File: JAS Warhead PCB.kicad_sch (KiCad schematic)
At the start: 7 parts, among them J1 Conn_01x15_Socket, J2 Conn_01x15_Socket, J3 Conn_01x02_Socket, J4 Conn_01x02_Socket, J5 Conn_01x02_Socket, J6 Conn_01x02_Socket, J7 Conn_01x02_Socket

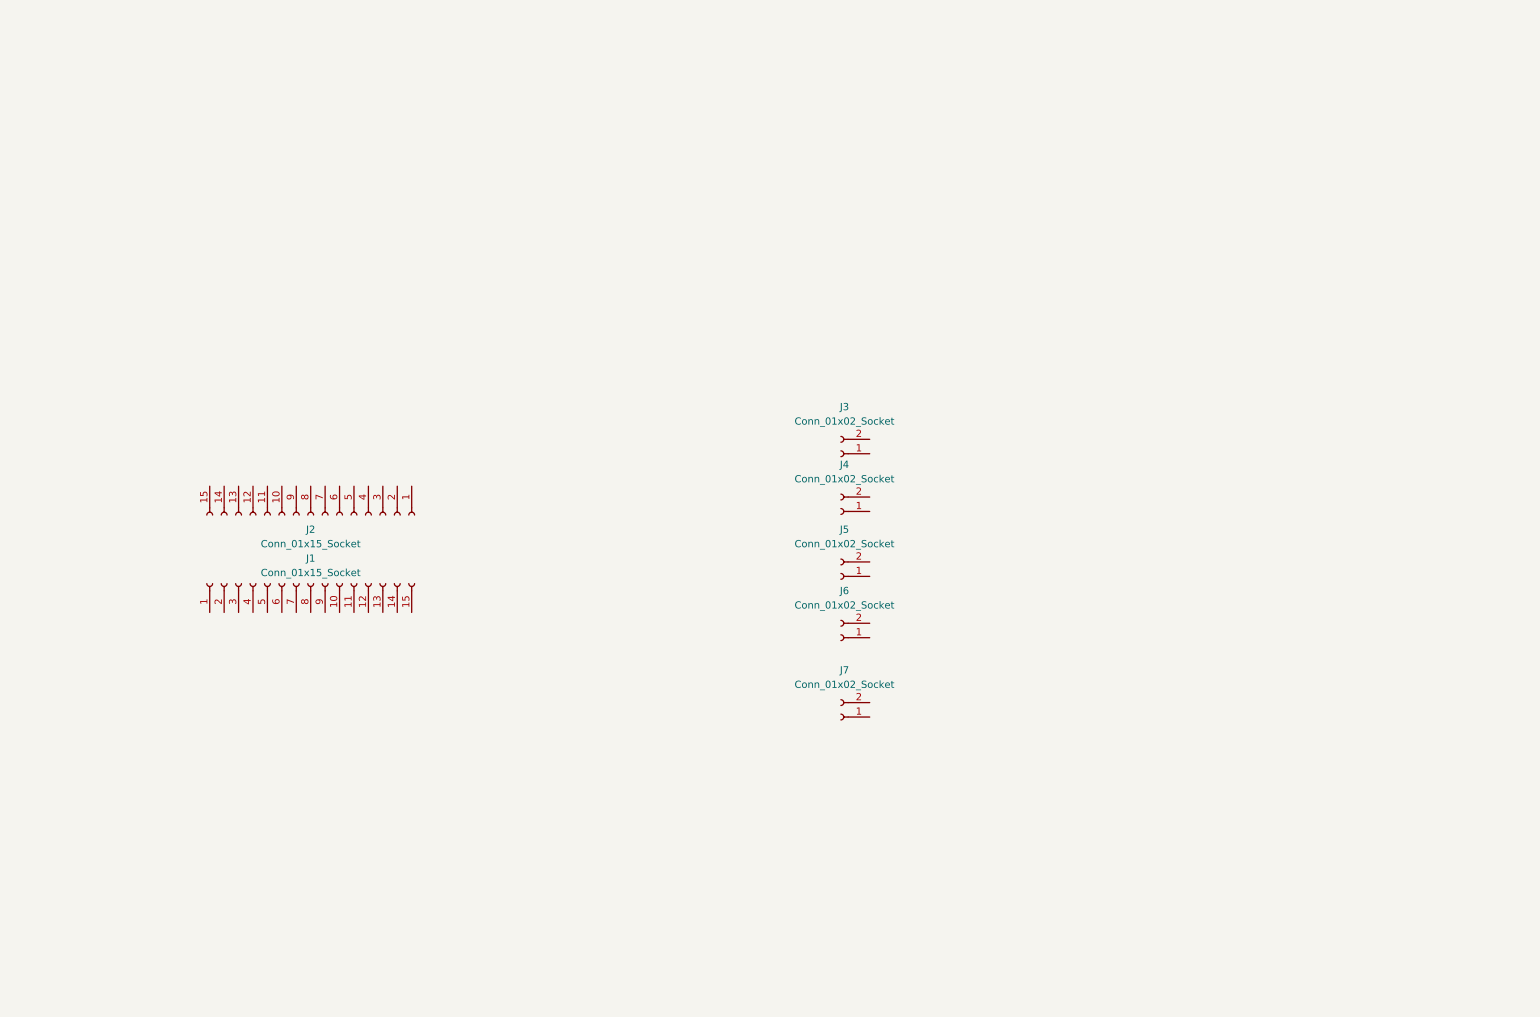
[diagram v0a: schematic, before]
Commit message: adds MAX31855 SPI K-Type Thermocouple Amps
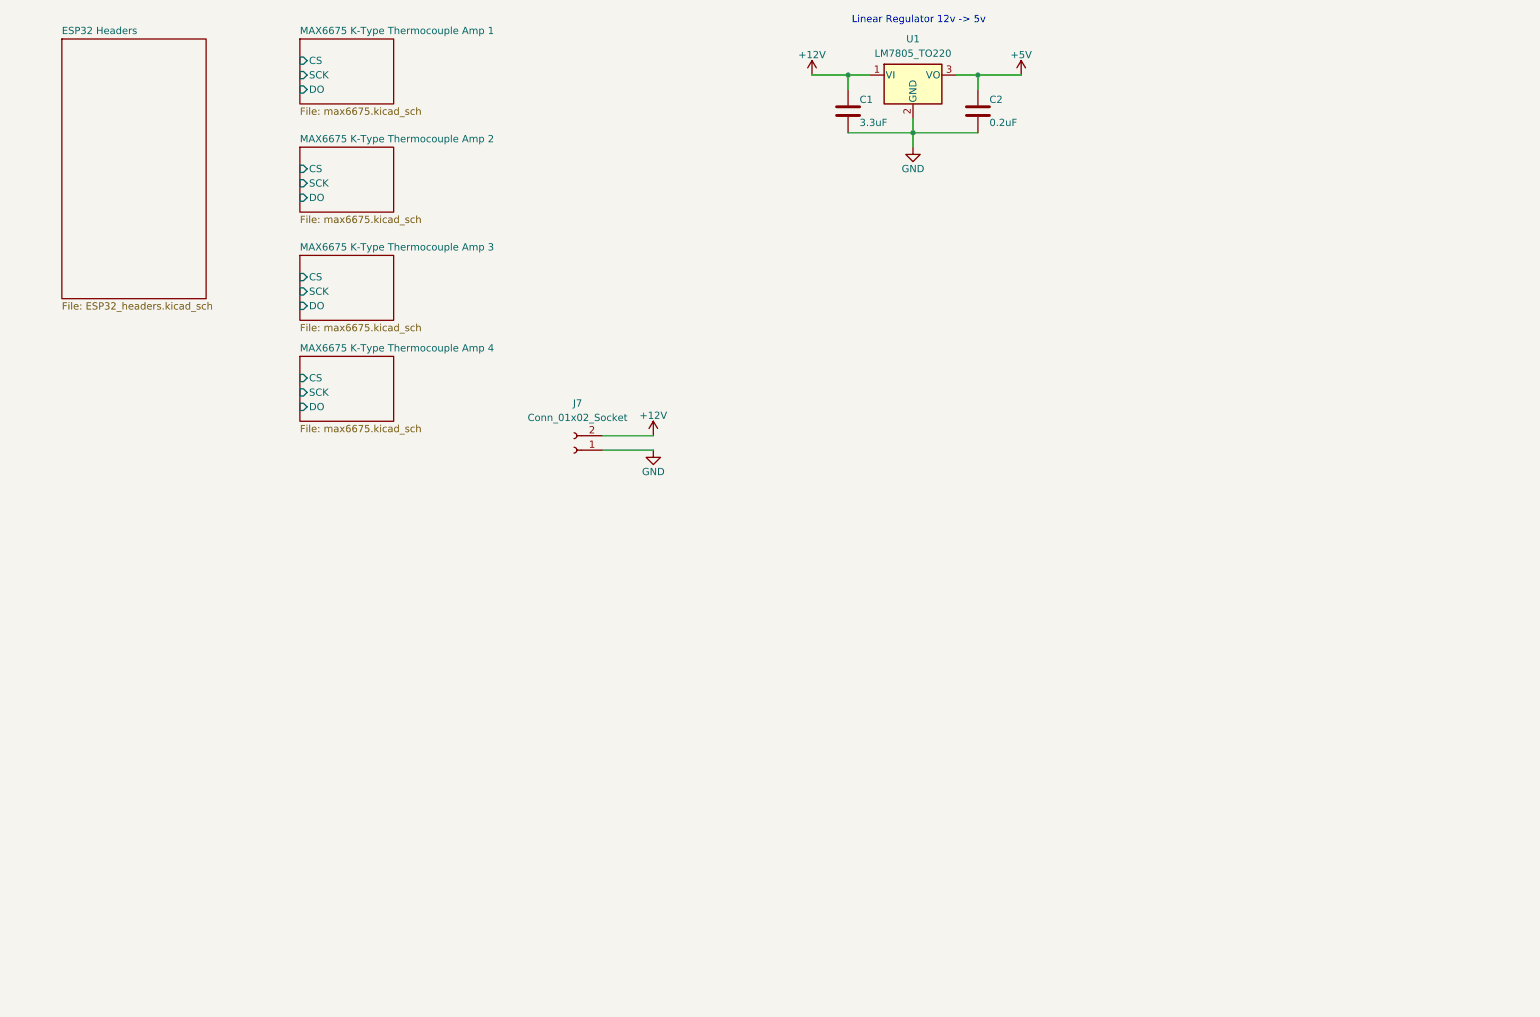
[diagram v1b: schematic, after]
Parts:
- removed J1, J2: Conn_01x15_Socket, Connector_PinSocket_2.54mm:PinSocket_1x15_P2.54mm_Vertical, symbol Connector:Conn_01x15_Socket
- removed J3, J4, J5, J6: Conn_01x02_Socket, TerminalBlock_4Ucon:TerminalBlock_4Ucon_1x02_P3.50mm_Horizontal, symbol Connector:Conn_01x02_Socket
- added C1: 3.3uF, Capacitor_SMD:C_0504_1310Metric, symbol Device:C
- added C2: 0.2uF, Capacitor_SMD:C_0402_1005Metric, symbol Device:C
- added U1: LM7805_TO220, Package_TO_SOT_THT:TO-220-3_Vertical, symbol Regulator_Linear:LM7805_TO220
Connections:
- net GND: now reaches J7.1 (Pin_1)
- net GND: now also C1.2, C2.2, U1.2 (GND)
- net +12V: now reaches J7.2 (Pin_2)
- net +12V: now also C1.1, U1.1 (VI)
- new net +5V: C2.1, U1.3 (VO)
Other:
- added sheet ESP32 Headers (ESP32_headers.kicad_sch)
- added sheet MAX6675 K-Type Thermocouple Amp 1 (max6675.kicad_sch)
- added sheet MAX6675 K-Type Thermocouple Amp 2 (max6675.kicad_sch)
- added sheet MAX6675 K-Type Thermocouple Amp 3 (max6675.kicad_sch)
- added sheet MAX6675 K-Type Thermocouple Amp 4 (max6675.kicad_sch)
- note added: "Linear Regulator 12v -> 5v"
- moved on the sheet: J7

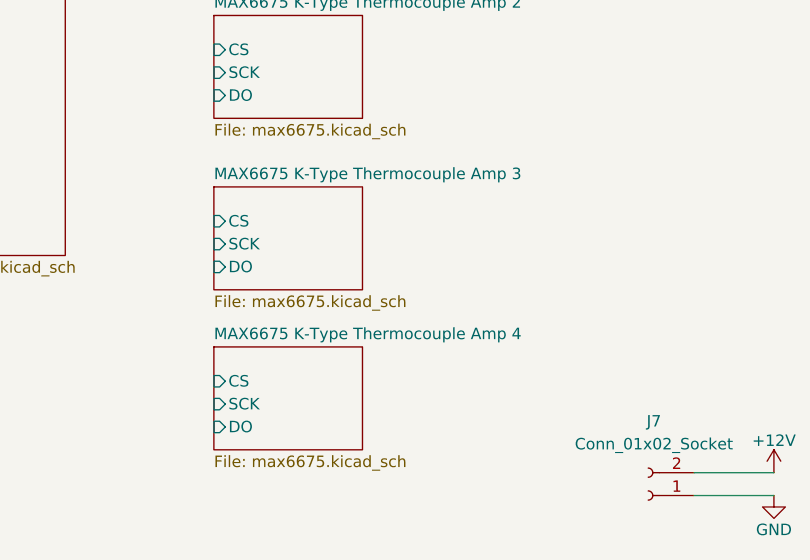
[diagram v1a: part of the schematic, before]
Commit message: finalizes MAX boards & Begins PCB Design
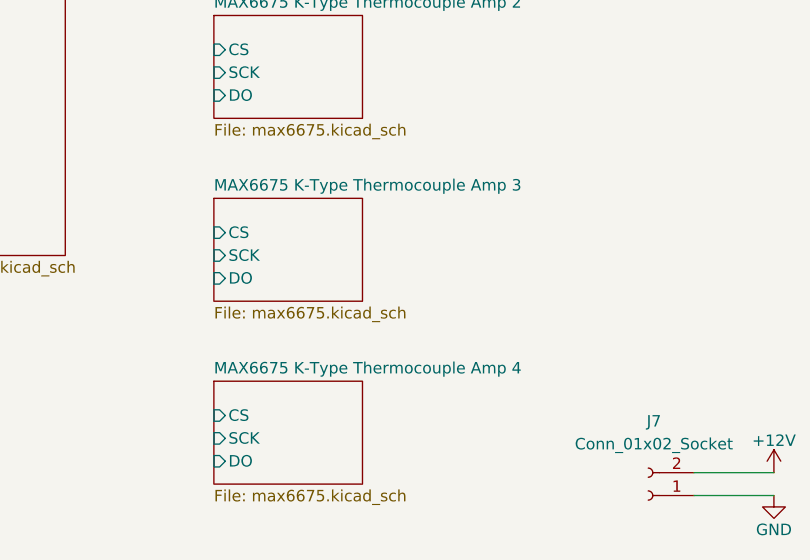
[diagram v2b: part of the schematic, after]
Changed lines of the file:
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@@
 	)
 	(sheet
-		(at 69.85 76.2)
+		(at 69.85 39.37)
+		(size 16.51 11.43)
+		(fields_autoplaced yes)
+		(stroke
+			(width 0.1524)
+			(type solid)
+		)
+		(fill
+			(color 0 0 0 0.0000)
+		)
+		(property "Sheetname" "MAX6675 K-Type Thermocouple Amp 2"
+			(at 69.85 38.6584 0)
+			(effects
+				(font
+					(size 1.27 1.27)
+				)
+				(justify left bottom)
+			)
+		)
+		(property "Sheetfile" "max6675.kicad_sch"
+			(at 69.85 51.3846 0)
+			(effects
+				(font
+					(size 1.27 1.27)
+				)
+				(justify left top)
+			)
+		)
+		(pin "CS" input
+			(at 69.85 43.18 180)
+			(effects
+				(font
+					(size 1.27 1.27)
+				)
+				(justify left)
+			)
+		)
+		(pin "SCK" input
+			(at 69.85 45.72 180)
+			(effects
+				(font
+					(size 1.27 1.27)
+				)
+				(justify left)
+			)
+		)
+		(pin "DO" input
+			(at 69.85 48.26 180)
+			(effects
+				(font
+					(size 1.27 1.27)
+				)
+				(justify left)
+			)
+		)
+		(instances
+			(project "JAS Warhead PCB"
+				(path "/a037544f-9a20-478c-bac0-d162f9edf245"
+					(page "4")
+				)
+			)
+		)
+	)
+	(sheet
+		(at 69.85 59.69)
+		(size 16.51 11.43)
+		(fields_autoplaced yes)
+		(stroke
+			(width 0.1524)
+			(type solid)
+		)
+		(fill
+			(color 0 0 0 0.0000)
+		)
+		(property "Sheetname" "MAX6675 K-Type Thermocouple Amp 3"
+			(at 69.85 58.9784 0)
+			(effects
+				(font
+					(size 1.27 1.27)
+				)
+				(justify left bottom)
+			)
+		)
+		(property "Sheetfile" "max6675.kicad_sch"
+			(at 69.85 71.7046 0)
+			(effects
+				(font
+					(size 1.27 1.27)
+				)
+				(justify left top)
+			)
+		)
+		(pin "CS" input
+			(at 69.85 63.5 180)
+			(effects
+				(font
+					(size 1.27 1.27)
+				)
+				(justify left)
+			)
+		)
+		(pin "SCK" input
+			(at 69.85 66.04 180)
+			(effects
+				(font
+					(size 1.27 1.27)
+				)
+				(justify left)
+			)
+		)
+		(pin "DO" input
+			(at 69.85 68.58 180)
+			(effects
+				(font
+					(size 1.27 1.27)
+				)
+				(justify left)
+			)
+		)
+		(instances
+			(project "JAS Warhead PCB"
+				(path "/a037544f-9a20-478c-bac0-d162f9edf245"
+					(page "5")
+				)
+			)
+		)
+	)
+	(sheet
+		(at 69.85 80.01)
 		(size 16.51 11.43)
 		(fields_autoplaced yes)
@@
 		)
 		(property "Sheetname" "MAX6675 K-Type Thermocouple Amp 4"
-			(at 69.85 75.4884 0)
-			(effects
-				(font
-					(size 1.27 1.27)
-				)
-				(justify left bottom)
-			)
-		)
-		(property "Sheetfile" "max6675.kicad_sch"
-			(at 69.85 88.2146 0)
-			(effects
-				(font
-					(size 1.27 1.27)
-				)
-				(justify left top)
-			)
-		)
-		(pin "CS" input
-			(at 69.85 80.01 180)
-			(effects
-				(font
-					(size 1.27 1.27)
-				)
-				(justify left)
-			)
-		)
-		(pin "SCK" input
-			(at 69.85 82.55 180)
-			(effects
-				(font
-					(size 1.27 1.27)
-				)
-				(justify left)
-			)
-		)
-		(pin "DO" input
-			(at 69.85 85.09 180)
+			(at 69.85 79.2984 0)
+			(effects
+				(font
+					(size 1.27 1.27)
+				)
+				(justify left bottom)
+			)
+		)
+		(property "Sheetfile" "max6675.kicad_sch"
+			(at 69.85 92.0246 0)
+			(effects
+				(font
+					(size 1.27 1.27)
+				)
+				(justify left top)
+			)
+		)
+		(pin "CS" input
+			(at 69.85 83.82 180)
+			(effects
+				(font
+					(size 1.27 1.27)
+				)
+				(justify left)
+			)
+		)
+		(pin "SCK" input
+			(at 69.85 86.36 180)
+			(effects
+				(font
+					(size 1.27 1.27)
+				)
+				(justify left)
+			)
+		)
+		(pin "DO" input
+			(at 69.85 88.9 180)
 			(effects
 				(font
@@
 				(path "/a037544f-9a20-478c-bac0-d162f9edf245"
 					(page "6")
-				)
-			)
-		)
-	)
-	(sheet
-		(at 69.85 58.42)
-		(size 16.51 11.43)
-		(fields_autoplaced yes)
-		(stroke
-			(width 0.1524)
-			(type solid)
-		)
-		(fill
-			(color 0 0 0 0.0000)
-		)
-		(property "Sheetname" "MAX6675 K-Type Thermocouple Amp 3"
-			(at 69.85 57.7084 0)
-			(effects
-				(font
-					(size 1.27 1.27)
-				)
-				(justify left bottom)
-			)
-		)
-		(property "Sheetfile" "max6675.kicad_sch"
-			(at 69.85 70.4346 0)
-			(effects
-				(font
-					(size 1.27 1.27)
-				)
-				(justify left top)
-			)
-		)
-		(pin "CS" input
-			(at 69.85 62.23 180)
-			(effects
-				(font
-					(size 1.27 1.27)
-				)
-				(justify left)
-			)
-		)
-		(pin "SCK" input
-			(at 69.85 64.77 180)
-			(effects
-				(font
-					(size 1.27 1.27)
-				)
-				(justify left)
-			)
-		)
-		(pin "DO" input
-			(at 69.85 67.31 180)
-			(effects
-				(font
-					(size 1.27 1.27)
-				)
-				(justify left)
-			)
-		)
-		(instances
-			(project "JAS Warhead PCB"
-				(path "/a037544f-9a20-478c-bac0-d162f9edf245"
-					(page "5")
 				)
 			)
@@
 				)
 			)
-		)
-	)
-	(sheet
-		(at 69.85 39.37)
-		(size 16.51 11.43)
-		(fields_autoplaced yes)
-		(stroke
-			(width 0.1524)
-			(type solid)
-		)
-		(fill
-			(color 0 0 0 0.0000)
-		)
-		(property "Sheetname" "MAX6675 K-Type Thermocouple Amp 2"
-			(at 69.85 38.6584 0)
-			(effects
-				(font
-					(size 1.27 1.27)
-				)
-				(justify left bottom)
-			)
-		)
-		(property "Sheetfile" "max6675.kicad_sch"
-			(at 69.85 51.3846 0)
-			(effects
-				(font
-					(size 1.27 1.27)
-				)
-				(justify left top)
-			)
-		)
-		(pin "CS" input
-			(at 69.85 43.18 180)
-			(effects
-				(font
-					(size 1.27 1.27)
-				)
-				(justify left)
-			)
-		)
-		(pin "SCK" input
-			(at 69.85 45.72 180)
-			(effects
-				(font
-					(size 1.27 1.27)
-				)
-				(justify left)
-			)
-		)
-		(pin "DO" input
-			(at 69.85 48.26 180)
-			(effects
-				(font
-					(size 1.27 1.27)
-				)
-				(justify left)
-			)
-		)
-		(instances
-			(project "JAS Warhead PCB"
-				(path "/a037544f-9a20-478c-bac0-d162f9edf245"
-					(page "4")
-				)
-			)

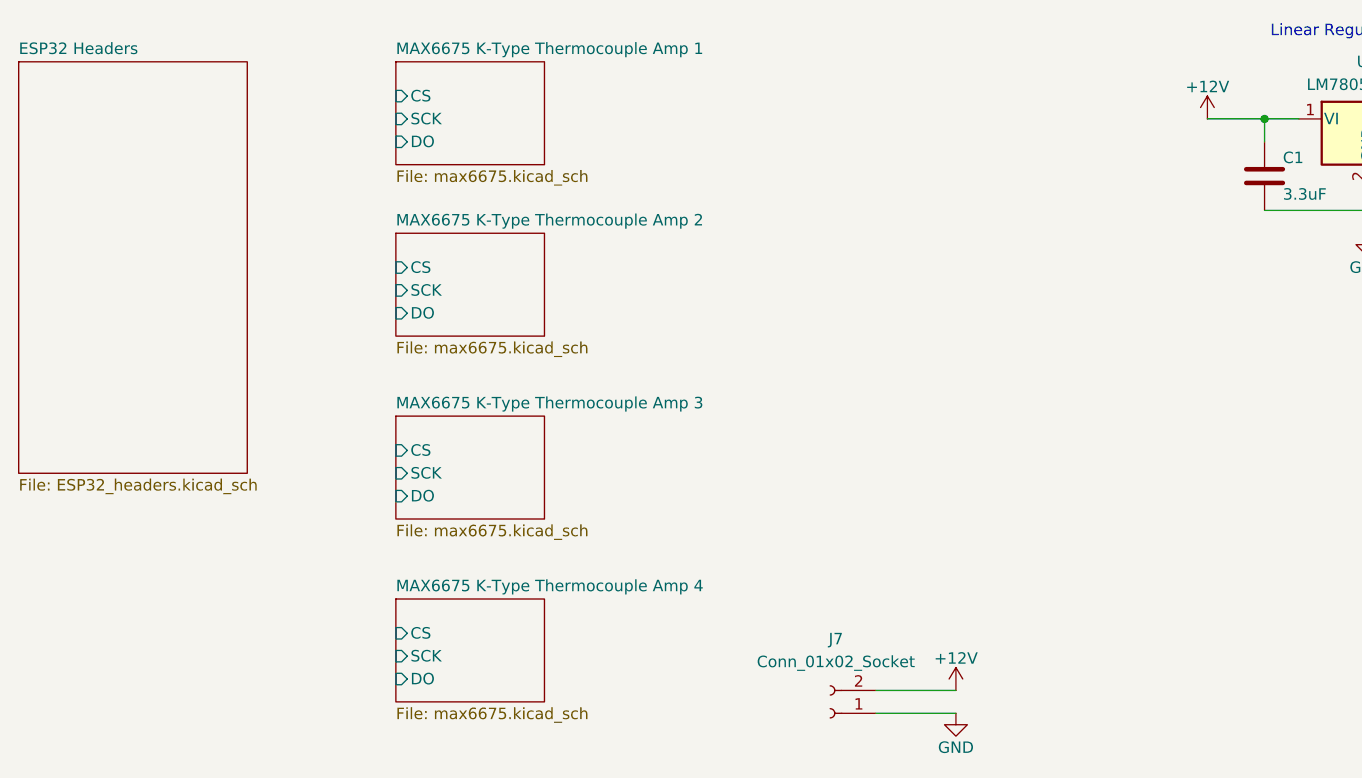
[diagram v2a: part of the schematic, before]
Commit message: PCB Wiring to ESP32
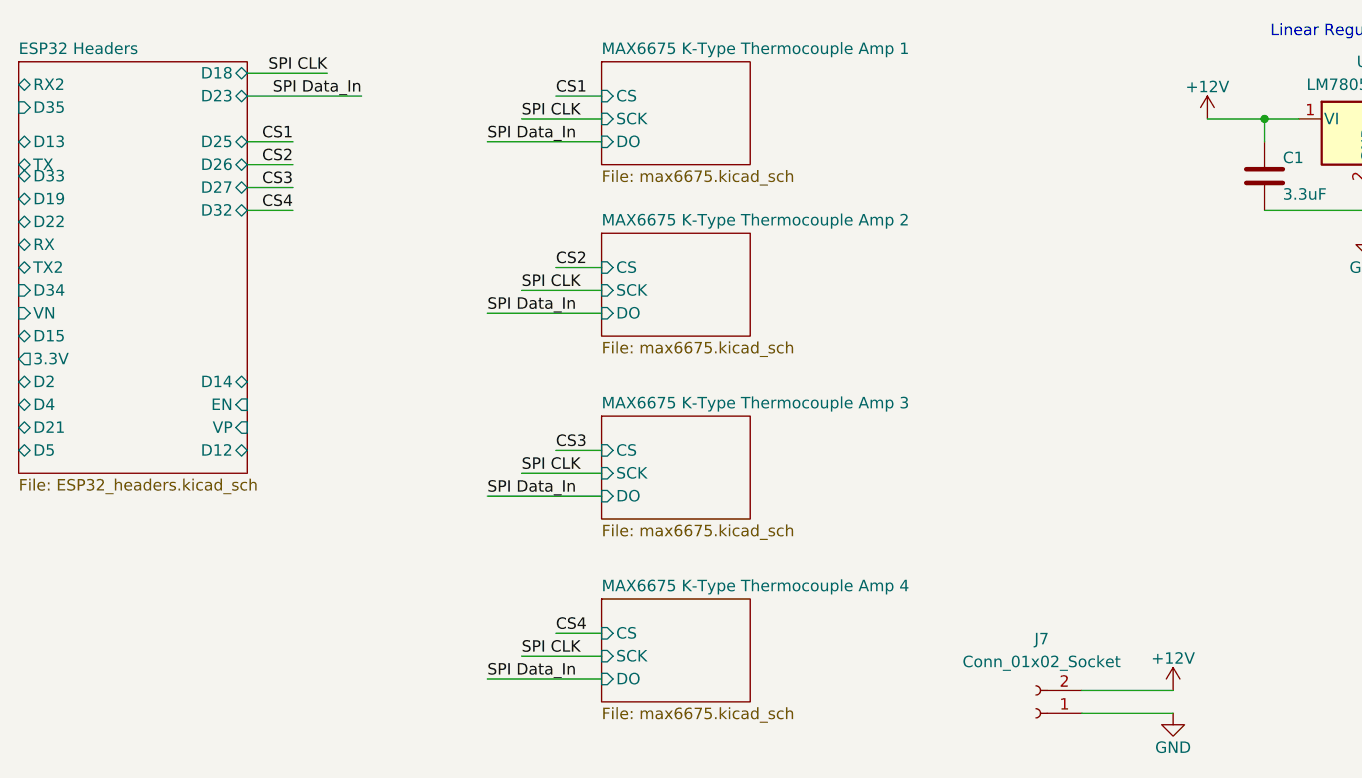
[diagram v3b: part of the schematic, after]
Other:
- sheet ESP32 Headers ports: added 3.3V, D12, D13, D14, D15, D18, D19, D2, D21, D22, D23, D25, D26, D27, D32, D33, D34, D35, D4, D5, EN, RX, RX2, TX, TX2, VN, VP; removed none
- moved on the sheet: J7

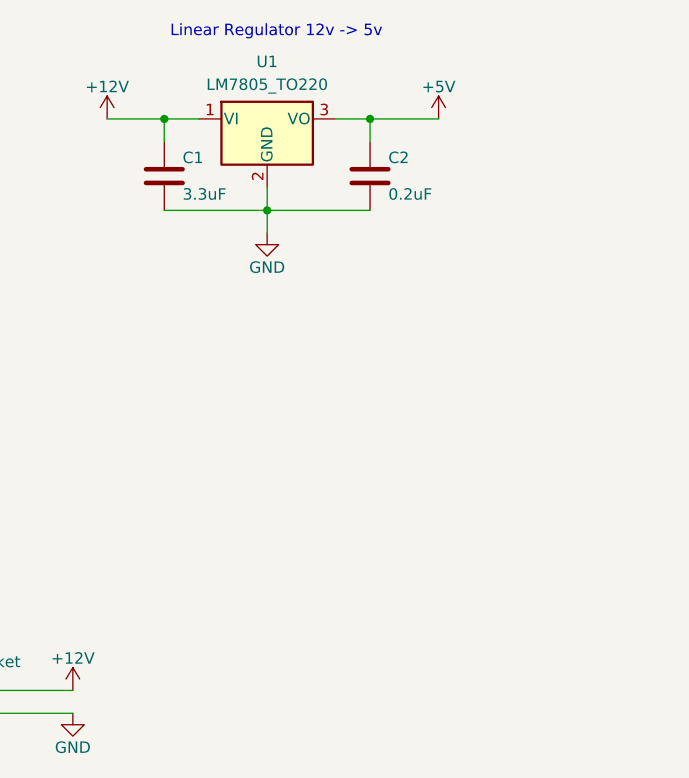
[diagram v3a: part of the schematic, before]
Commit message: mounting holes
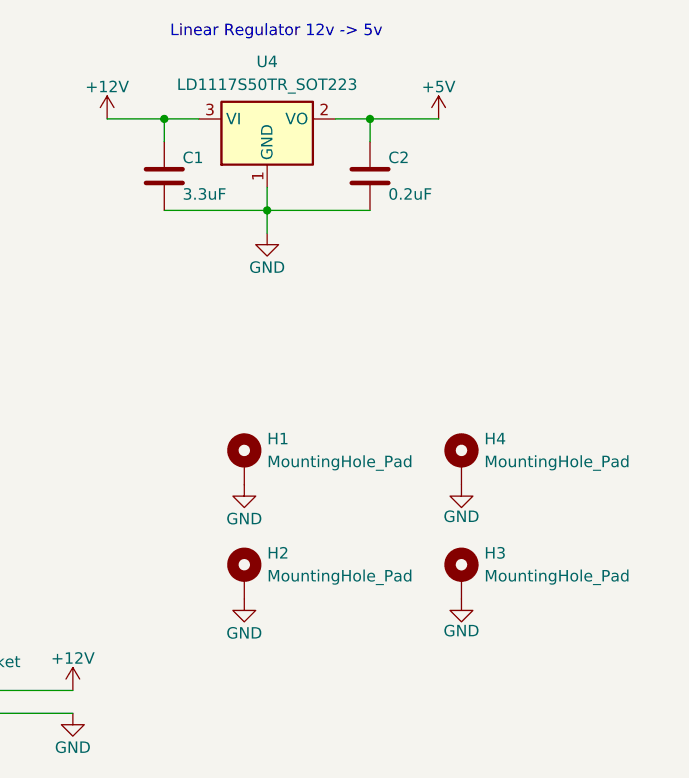
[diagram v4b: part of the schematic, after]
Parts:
- removed U1: LM7805_TO220, Package_TO_SOT_THT:TO-220-3_Vertical, symbol Regulator_Linear:LM7805_TO220
- added H1, H2, H3, H4: MountingHole_Pad, MountingHole:MountingHole_4.3mm_M4_DIN965_Pad, symbol Mechanical:MountingHole_Pad
- added U4: LD1117S50TR_SOT223, Package_TO_SOT_SMD:SOT-223-3_TabPin2, symbol Regulator_Linear:LD1117S50TR_SOT223
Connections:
- net +12V: now also U4.3 (VI)
- net +5V: now also U4.2 (VO)
- net GND: now also H1.1, H2.1, H3.1, H4.1, U4.1 (GND)
